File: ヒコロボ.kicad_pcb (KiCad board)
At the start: 2 copper layers, 96.5 x 29.5 mm, 7 parts, among them U1 R3106GF, U2 4053, U3 4053, U5 R3106FG_IF

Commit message: update pcb setting
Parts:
- moved U2 1.27 mm to (87.6, 101.6)
- moved U3 1.27 mm to (87.6, 86.4)
- moved U5 1.06 mm to (63.1, 87.1)
- moved U1 1.06 mm to (72.2, 92.7)
- moved U4 1.06 mm to (63.0, 98.6)
- moved U6 1.06 mm to (63.0, 102.9)
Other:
- board size 96.5 x 29.5 mm -> 94 x 29.5 mm
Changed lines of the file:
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@@
 		(capping no)
 		(filling no)
-		(zone_defaults)
 		(pcbplotparams
 			(layerselection 0x00000000_00000000_55555555_5755f5ff)
@@
 	(footprint "Library:DIP794W45P254L1969H508Q16"
 		(layer "F.Cu")
-		(at 86.36 101.6 90)
+		(at 87.63 101.6 90)
 		(property "Reference" "U2"
 			(at -1.425 -10.835 90)
@@
 	(footprint "Library:R3106FG"
 		(layer "F.Cu")
-		(at 71.12 92.71 -90)
+		(at 72.176 92.71 -90)
 		(property "Reference" "U1"
 			(at 0 -4.572 270)
@@
 	(footprint "Library:R3106FG"
 		(layer "F.Cu")
-		(at 62.016 87.122 -90)
+		(at 63.072 87.122 -90)
 		(property "Reference" "U5"
 			(at 0 -4.572 270)
@@
 	(footprint "Library:Sensor_IF"
 		(layer "F.Cu")
-		(at 61.939 102.87)
+		(at 62.995 102.87)
 		(property "Reference" "U6"
 			(at 0 -0.5 0)
@@
 	(footprint "Library:DIP794W45P254L1969H508Q16"
 		(layer "F.Cu")
-		(at 86.36 86.36 90)
+		(at 87.63 86.36 90)
 		(property "Reference" "U3"
 			(at -1.425 -10.835 90)
@@
 	(footprint "Library:Sensor_IF"
 		(layer "F.Cu")
-		(at 61.976 98.552)
+		(at 63.032 98.552)
 		(property "Reference" "U4"
 			(at 0 -0.5 0)
@@
 	)
 	(gr_rect
-		(start 55.88 78.74)
+		(start 58.42 78.74)
 		(end 152.4 108.204)
 		(stroke

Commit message: pcb changed
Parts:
- moved U2 1.27 mm to (87.6, 100.3)
- moved U3 1.02 mm to (87.6, 87.4)
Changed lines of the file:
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@@
 	(footprint "Library:DIP794W45P254L1969H508Q16"
 		(layer "F.Cu")
-		(at 87.63 101.6 90)
+		(at 87.63 100.33 90)
 		(property "Reference" "U2"
 			(at -1.425 -10.835 90)
@@
 	(footprint "Library:DIP794W45P254L1969H508Q16"
 		(layer "F.Cu")
-		(at 87.63 86.36 90)
+		(at 87.63 87.376 90)
 		(property "Reference" "U3"
 			(at -1.425 -10.835 90)

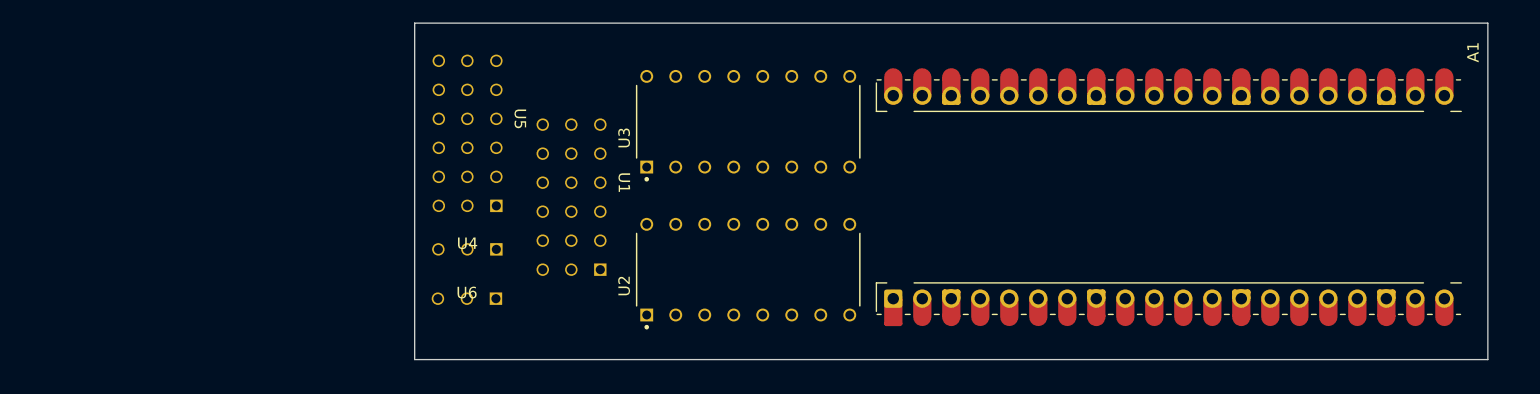
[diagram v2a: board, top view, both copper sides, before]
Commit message: update sensor IF
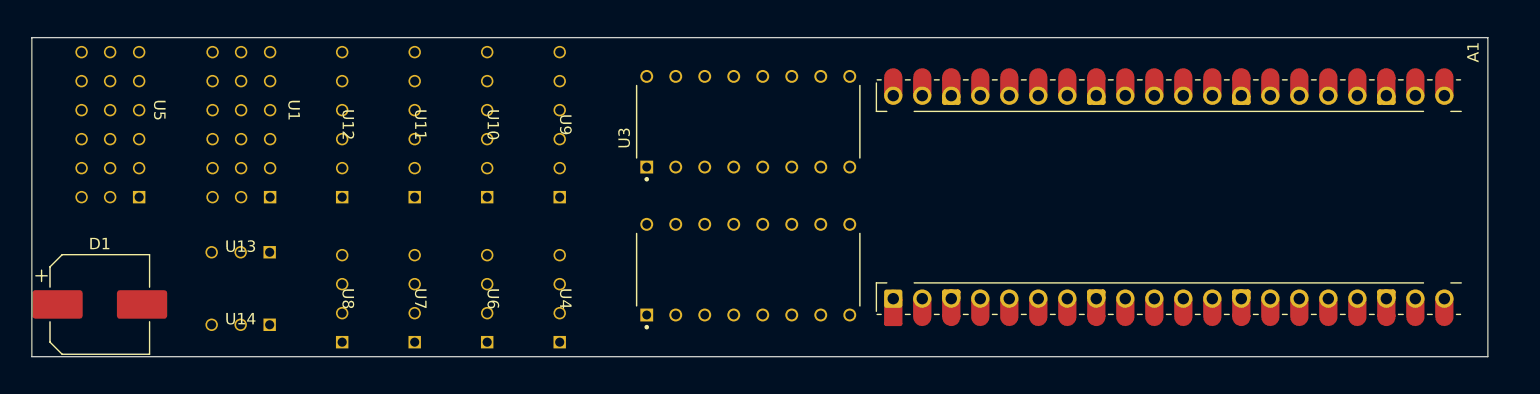
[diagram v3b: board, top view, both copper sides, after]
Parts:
- added D1: D_Capacitance, Capacitor_SMD:CP_Elec_8x10.5, F.Cu at (30.8, 103.4)
- added U10: ~, Library:Sensor_SPI_IF, F.Cu at (64.8, 87.6)
- added U11: ~, Library:Sensor_SPI_IF, F.Cu at (58.4, 87.6)
- added U12: ~, Library:Sensor_SPI_IF, F.Cu at (52.1, 87.6)
- added U13: ~, Library:Sensor_Analog_IF, F.Cu at (43.2, 98.8)
- added U14: ~, Library:Sensor_Analog_IF, F.Cu at (43.2, 105.2)
- added U7: ~, Library:Sensor_I2C_IF, F.Cu at (58.4, 102.9)
- added U8: ~, Library:Sensor_I2C_IF, F.Cu at (52.1, 102.9)
- added U9: ~, Library:Sensor_SPI_IF, F.Cu at (71.1, 87.6)
- U4, U6: footprint Library:Sensor_IF -> Library:Sensor_I2C_IF
- moved U5 31.3 mm to (31.8, 86.4)
- moved U1 29.6 mm to (43.3, 86.4)
- moved U4 9.17 mm to (71.1, 102.9), turned to -90 degrees
- moved U6 1.77 mm to (64.8, 102.9), turned to -90 degrees
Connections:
- A1 pad 22: unconnected-(A1-GPIO17-Pad22) -> Net-(A1-GPIO17)
- A1 pad 24: unconnected-(A1-GPIO18-Pad24) -> Net-(A1-GPIO18)
- A1 pad 32: unconnected-(A1-GPIO27_ADC1-Pad32) -> Net-(A1-GPIO27_ADC1)
- A1 pad 33: unconnected-(A1-AGND-Pad33) -> Net-(A1-AGND)
- A1 pad 34: unconnected-(A1-GPIO28_ADC2-Pad34) -> Net-(A1-GPIO28_ADC2)
- U1 pad 1: Net-(A1-GPIO12) -> Net-(A1-GPIO7)
- U1 pad 2: Net-(A1-GPIO13) -> Net-(A1-GPIO8)
- U1 pad 3: Net-(A1-GPIO14) -> Net-(A1-GPIO9)
- U1 pad 4: Net-(A1-GPIO15) -> Net-(A1-GPIO10)
- U1 pad 5: Net-(A1-GPIO22) -> Net-(A1-GPIO11)
- U1 pad 6: Net-(A1-GPIO21) -> Net-(A1-GPIO12)
- U2 pad 1: Net-(A1-GPIO7) -> Net-(A1-GPIO2)
- U2 pad 10: Net-(A1-GPIO1) -> Net-(A1-GPIO0)
- U2 pad 11: Net-(A1-GPIO2) -> Net-(A1-GPIO0)
- U2 pad 12: Net-(A1-GPIO15) -> Net-(A1-GPIO10)
- U2 pad 13: Net-(A1-GPIO8) -> Net-(A1-GPIO3)
- U2 pad 2: Net-(A1-GPIO22) -> Net-(A1-GPIO11)
- U2 pad 3: Net-(A1-GPIO6) -> Net-(A1-GPIO1)
- U2 pad 5: Net-(A1-GPIO21) -> Net-(A1-GPIO12)
- U3 pad 1: Net-(A1-GPIO10) -> Net-(A1-GPIO5)
- U3 pad 10: Net-(A1-GPIO4) -> Net-(A1-GPIO0)
- U3 pad 11: Net-(A1-GPIO5) -> Net-(A1-GPIO0)
- U3 pad 12: Net-(A1-GPIO12) -> Net-(A1-GPIO7)
- U3 pad 13: Net-(A1-GPIO11) -> Net-(A1-GPIO6)
- U3 pad 2: Net-(A1-GPIO13) -> Net-(A1-GPIO8)
- U3 pad 3: Net-(A1-GPIO9) -> Net-(A1-GPIO4)
- U3 pad 5: Net-(A1-GPIO14) -> Net-(A1-GPIO9)
- U3 pad 9: Net-(A1-GPIO3) -> Net-(A1-GPIO0)
- U4 pad 1: GND -> Net-(A1-GPIO13)
- U4 pad 2: +5V -> Net-(A1-GPIO14)
- U4 pad 3: Net-(A1-GPIO20) -> Net-(A1-3V3)
- U6 pad 1: GND -> Net-(A1-GPIO13)
- U6 pad 2: +5V -> Net-(A1-GPIO14)
- U6 pad 3: Net-(A1-GPIO19) -> Net-(A1-3V3)
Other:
- board size 94 x 29.5 mm -> 127.5 x 27.9 mm

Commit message: wired and clear JLCPCB design rule
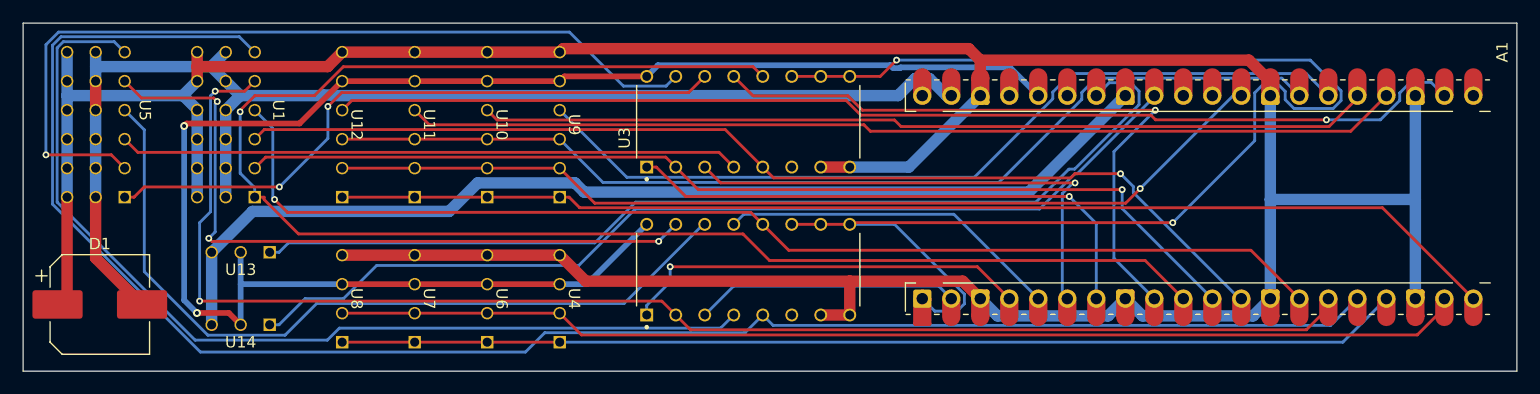
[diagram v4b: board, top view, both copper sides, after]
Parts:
- moved A1 2.54 mm to (127.0, 94.0)
- moved U1 1.35 mm to (41.9, 86.4)
- moved U5 1.27 mm to (30.5, 86.4)
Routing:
- net GND: track 0.00 -> 306.2 mm
- net Net-(A1-GPIO12): track 0.00 -> 155.6 mm
- net Net-(A1-3V3): track 0.00 -> 144.1 mm, vias 0 -> 2
- net Net-(A1-GPIO7): track 0.00 -> 141.7 mm, vias 0 -> 1
- net Net-(A1-GPIO0): track 0.00 -> 126.6 mm, vias 0 -> 2
- net Net-(A1-GPIO11): track 0.00 -> 124.3 mm, vias 0 -> 2
- net +5V: track 0.00 -> 113.1 mm
- net Net-(A1-GPIO15): track 0.00 -> 103.5 mm
- net Net-(A1-GPIO10): track 0.00 -> 102.7 mm, vias 0 -> 1
- net Net-(A1-GPIO17): track 0.00 -> 100.6 mm, vias 0 -> 1
- net Net-(A1-GPIO14): track 0.00 -> 99.1 mm
- net Net-(A1-GPIO9): track 0.00 -> 94.3 mm, vias 0 -> 1
- net Net-(A1-GPIO13): track 0.00 -> 93.8 mm
- net Net-(A1-AGND): track 0.00 -> 93.5 mm
- net Net-(A1-GPIO8): track 0.00 -> 91.2 mm, vias 0 -> 1
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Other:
- board size 127.5 x 27.9 mm -> 130.8 x 30.5 mm
